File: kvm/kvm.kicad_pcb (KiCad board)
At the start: 4 copper layers, 56.8 x 69.3 mm, 61 parts, among them J1 USB4110-GF-A, J2 USB4110-GF-A, J3 USB_A_Stacked, J4 USB_A_Stacked, Q1 Q_PMOS_GSD, SW1 SW_DPDT_x2, U1 SRV05-4, U2 LTC4412xS6, U3 FSUSB42MUX, U4 GL850G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

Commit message: added gerber files
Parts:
- moved F2 2.03 mm to (92.2, 72.8), turned to -90 degrees
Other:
- board size 56.8 x 69.3 mm -> 57 x 69.3 mm
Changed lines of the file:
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@@
       (layerselection 0x00010fc_ffffffff)
       (disableapertmacros false)
-      (usegerberextensions false)
+      (usegerberextensions true)
       (usegerberattributes true)
-      (usegerberadvancedattributes true)
-      (creategerberjobfile true)
+      (usegerberadvancedattributes false)
+      (creategerberjobfile false)
       (svguseinch false)
       (svgprecision 6)
@@
       (plotinvisibletext false)
       (sketchpadsonfab false)
-      (subtractmaskfromsilk false)
+      (subtractmaskfromsilk true)
       (outputformat 1)
       (mirror false)
-      (drillshape 1)
+      (drillshape 0)
       (scaleselection 1)
-      (outputdirectory "")
+      (outputdirectory "fabrication/")
     )
   )
@@
     (fp_line (start -1.6 0.8) (end -1.6 -0.8) (layer "F.Fab") (width 0.1))
     (fp_line (start 1.6 0.8) (end -1.6 0.8) (layer "F.Fab") (width 0.1))
-    (pad "1" smd roundrect (at -1.4875 0 180) (size 1.425 1.75) (layers "F.Cu" "F.Paste" "F.Mask") (roundrect_rratio 0.175439)
+    (pad "1" smd roundrect (at -1.4875 0 180) (size 1.425 1.75) (layers "F.Cu" "F.Paste" "F.Mask") (roundrect_rratio 0.1754392982)
       (net 1 "V5") (pintype "passive"))
-    (pad "2" smd roundrect (at 1.4875 0 180) (size 1.425 1.75) (layers "F.Cu" "F.Paste" "F.Mask") (roundrect_rratio 0.175439)
+    (pad "2" smd roundrect (at 1.4875 0 180) (size 1.425 1.75) (layers "F.Cu" "F.Paste" "F.Mask") (roundrect_rratio 0.1754392982)
       (net 14 "Net-(C16-Pad1)") (pintype "passive"))
     (model "${KICAD6_3DMODEL_DIR}/Fuse.3dshapes/Fuse_1206_3216Metric.wrl"
@@
     (fp_line (start 1 0.625) (end -1 0.625) (layer "F.Fab") (width 0.1))
     (fp_line (start -1 -0.625) (end 1 -0.625) (layer "F.Fab") (width 0.1))
-    (pad "1" smd roundrect (at -1.0375 0 90) (size 1.175 1.45) (layers "F.Cu" "F.Paste" "F.Mask") (roundrect_rratio 0.212766)
+    (pad "1" smd roundrect (at -1.0375 0 90) (size 1.175 1.45) (layers "F.Cu" "F.Paste" "F.Mask") (roundrect_rratio 0.2127659574)
       (net 3 "DVDD") (pintype "passive"))
-    (pad "2" smd roundrect (at 1.0375 0 90) (size 1.175 1.45) (layers "F.Cu" "F.Paste" "F.Mask") (roundrect_rratio 0.212766)
+    (pad "2" smd roundrect (at 1.0375 0 90) (size 1.175 1.45) (layers "F.Cu" "F.Paste" "F.Mask") (roundrect_rratio 0.2127659574)
       (net 2 "GND") (pintype "passive"))
     (model "${KICAD6_3DMODEL_DIR}/Capacitor_SMD.3dshapes/C_0805_2012Metric.wrl"
@@
     (fp_line (start -1 0.6) (end 1 0.6) (layer "F.Fab") (width 0.1))
     (fp_line (start -1 -0.3) (end -1 0.6) (layer "F.Fab") (width 0.1))
-    (pad "1" smd roundrect (at -1.025 0) (size 1.15 1.4) (layers "F.Cu" "F.Paste" "F.Mask") (roundrect_rratio 0.217391)
+    (pad "1" smd roundrect (at -1.025 0) (size 1.15 1.4) (layers "F.Cu" "F.Paste" "F.Mask") (roundrect_rratio 0.2173913043)
       (net 17 "PGANG") (pinfunction "K") (pintype "passive"))
-    (pad "2" smd roundrect (at 1.025 0) (size 1.15 1.4) (layers "F.Cu" "F.Paste" "F.Mask") (roundrect_rratio 0.217391)
+    (pad "2" smd roundrect (at 1.025 0) (size 1.15 1.4) (layers "F.Cu" "F.Paste" "F.Mask") (roundrect_rratio 0.2173913043)
       (net 18 "Net-(D2-Pad2)") (pinfunction "A") (pintype "passive"))
     (model "${KICAD6_3DMODEL_DIR}/LED_SMD.3dshapes/LED_0805_2012Metric.wrl"
@@
     (fp_line (start -1.6 0.8) (end -1.6 -0.8) (layer "F.Fab") (width 0.1))
     (fp_line (start -1.6 -0.8) (end 1.6 -0.8) (layer "F.Fab") (width 0.1))
-    (pad "1" smd roundrect (at -1.4875 0 180) (size 1.425 1.75) (layers "F.Cu" "F.Paste" "F.Mask") (roundrect_rratio 0.175439)
+    (pad "1" smd roundrect (at -1.4875 0 180) (size 1.425 1.75) (layers "F.Cu" "F.Paste" "F.Mask") (roundrect_rratio 0.1754392982)
       (net 1 "V5") (pintype "passive"))
-    (pad "2" smd roundrect (at 1.4875 0 180) (size 1.425 1.75) (layers "F.Cu" "F.Paste" "F.Mask") (roundrect_rratio 0.175439)
+    (pad "2" smd roundrect (at 1.4875 0 180) (size 1.425 1.75) (layers "F.Cu" "F.Paste" "F.Mask") (roundrect_rratio 0.1754392982)
       (net 7 "Net-(C4-Pad1)") (pintype "passive"))
     (model "${KICAD6_3DMODEL_DIR}/Fuse.3dshapes/Fuse_1206_3216Metric.wrl"
@@
   )
   (footprint "Fuse:Fuse_1206_3216Metric_Pad1.42x1.75mm_HandSolder" (layer "F.Cu")
-    (at 93.599 74.23801 180)
+    (at 92.202 72.771 -90)
     (descr "Fuse SMD 1206 (3216 Metric), square (rectangular) end terminal, IPC_7351 nominal with elongated pad for handsoldering. (Body size source: http://www.tortai-tech.com/upload/download/2011102023233369053.pdf), generated with kicad-footprint-generator")
     (tags "fuse handsolder")
@@
     (property "Sheetname" "")
     (attr smd)
-    (fp_text reference "F2" (at 0 -1.82) (layer "F.SilkS")
+    (fp_text reference "F2" (at 0 -1.82 -270) (layer "F.SilkS")
       (effects (font (size 1 1) (thickness 0.15)))
     )
-    (fp_text value "Polyfuse" (at 0 1.82) (layer "F.Fab")
+    (fp_text value "Polyfuse" (at 0 1.82 -270) (layer "F.Fab")
       (effects (font (size 1 1) (thickness 0.15)))
     )
-    (fp_text user "${REFERENCE}" (at 0 0) (layer "F.Fab")
+    (fp_text user "${REFERENCE}" (at 0 0 -270) (layer "F.Fab")
       (effects (font (size 0.8 0.8) (thickness 0.12)))
     )
@@
     (fp_line (start -1.6 0.8) (end -1.6 -0.8) (layer "F.Fab") (width 0.1))
     (fp_line (start 1.6 0.8) (end -1.6 0.8) (layer "F.Fab") (width 0.1))
-    (pad "1" smd roundrect (at -1.4875 0 180) (size 1.425 1.75) (layers "F.Cu" "F.Paste" "F.Mask") (roundrect_rratio 0.175439)
+    (pad "1" smd roundrect (at -1.4875 0 270) (size 1.425 1.75) (layers "F.Cu" "F.Paste" "F.Mask") (roundrect_rratio 0.1754392982)
       (net 1 "V5") (pintype "passive"))
-    (pad "2" smd roundrect (at 1.4875 0 180) (size 1.425 1.75) (layers "F.Cu" "F.Paste" "F.Mask") (roundrect_rratio 0.175439)
+    (pad "2" smd roundrect (at 1.4875 0 270) (size 1.425 1.75) (layers "F.Cu" "F.Paste" "F.Mask") (roundrect_rratio 0.1754392982)
       (net 9 "Net-(C6-Pad1)") (pintype "passive"))
     (model "${KICAD6_3DMODEL_DIR}/Fuse.3dshapes/Fuse_1206_3216Metric.wrl"
@@
     (fp_line (start -1.6 0.8) (end -1.6 -0.8) (layer "F.Fab") (width 0.1))
     (fp_line (start -1.6 -0.8) (end 1.6 -0.8) (layer "F.Fab") (width 0.1))
-    (pad "1" smd roundrect (at -1.4875 0 180) (size 1.425 1.75) (layers "F.Cu" "F.Paste" "F.Mask") (roundrect_rratio 0.175439)
+    (pad "1" smd roundrect (at -1.4875 0 180) (size 1.425 1.75) (layers "F.Cu" "F.Paste" "F.Mask") (roundrect_rratio 0.1754392982)
       (net 1 "V5") (pintype "passive"))
-    (pad "2" smd roundrect (at 1.4875 0 180) (size 1.425 1.75) (layers "F.Cu" "F.Paste" "F.Mask") (roundrect_rratio 0.175439)
+    (pad "2" smd roundrect (at 1.4875 0 180) (size 1.425 1.75) (layers "F.Cu" "F.Paste" "F.Mask") (roundrect_rratio 0.1754392982)
       (net 15 "Net-(C17-Pad1)") (pintype "passive"))
     (model "${KICAD6_3DMODEL_DIR}/Fuse.3dshapes/Fuse_1206_3216Metric.wrl"
@@
     )
   )
-  (gr_rect (start 116.713 39.37) (end 59.944 108.712) (layer "Edge.Cuts") (width 0.1) (fill none))
+  (gr_rect (start 116.713 39.37) (end 59.69 108.712) (layer "Edge.Cuts") (width 0.1) (fill none))
   (gr_text "K(V)M - USB Hub\n" (at 104.394 42.926) (layer "F.SilkS")
     (effects (font (size 1.5 1.5) (thickness 0.3)))
@@
     (effects (font (size 1.5 1.5) (thickness 0.3)))
   )
+  (segment (start 92.202 71.2835) (end 92.202 69.469) (width 0.8) (layer "F.Cu") (net 1))
   (segment (start 81.915 48.514) (end 81.207512 48.514) (width 0.8) (layer "F.Cu") (net 1))
   (segment (start 85.524 48.3605) (end 85.3705 48.514) (width 0.8) (layer "F.Cu") (net 1))
-  (segment (start 95.0865 74.23801) (end 96.32299 74.23801) (width 0.8) (layer "F.Cu") (net 1))
   (segment (start 107.8821 59.0962) (end 109.4328 59.0962) (width 0.25) (layer "F.Cu") (net 1))
   (segment (start 109.4328 59.0962) (end 109.474 59.055) (width 0.25) (layer "F.Cu") (net 1))
@@
   (segment (start 88.4825 68.199) (end 90.043 68.199) (width 0.8) (layer "F.Cu") (net 1))
   (segment (start 81.1795 44.355908) (end 80.1665 43.342908) (width 0.8) (layer "F.Cu") (net 1))
-  (segment (start 96.32299 74.23801) (end 96.52 74.041) (width 0.8) (layer "F.Cu") (net 1))
   (segment (start 85.3705 48.514) (end 85.725 48.8685) (width 0.6) (layer "F.Cu") (net 1))
   (segment (start 81.1795 47.5985) (end 81.1795 44.355908) (width 0.8) (layer "F.Cu") (net 1))
@@
   (segment (start 86.1325 48.3605) (end 85.524 48.3605) (width 0.8) (layer "F.Cu") (net 1))
   (segment (start 92.1655 89.662) (end 93.853 89.662) (width 0.8) (layer "F.Cu") (net 1))
+  (via (at 92.202 69.469) (size 0.8) (drill 0.4) (layers "F.Cu" "B.Cu") (net 1))
   (via (at 86.868 83.947) (size 0.8) (drill 0.4) (layers "F.Cu" "B.Cu") (net 1))
   (via (at 112.776 89.916) (size 0.8) (drill 0.4) (layers "F.Cu" "B.Cu") (net 1))
@@
   (via (at 90.1965 42.2645) (size 0.8) (drill 0.4) (layers "F.Cu" "B.Cu") (net 1))
   (via (at 88.0375 48.2335) (size 0.8) (drill 0.4) (layers "F.Cu" "B.Cu") (net 1))
-  (via (at 96.52 74.041) (size 0.8) (drill 0.4) (layers "F.Cu" "B.Cu") (net 1))
   (via (at 96.266 95.25) (size 0.8) (drill 0.4) (layers "F.Cu" "B.Cu") (net 1))
   (via (at 108.712 75.311) (size 0.8) (drill 0.4) (layers "F.Cu" "B.Cu") (net 1))

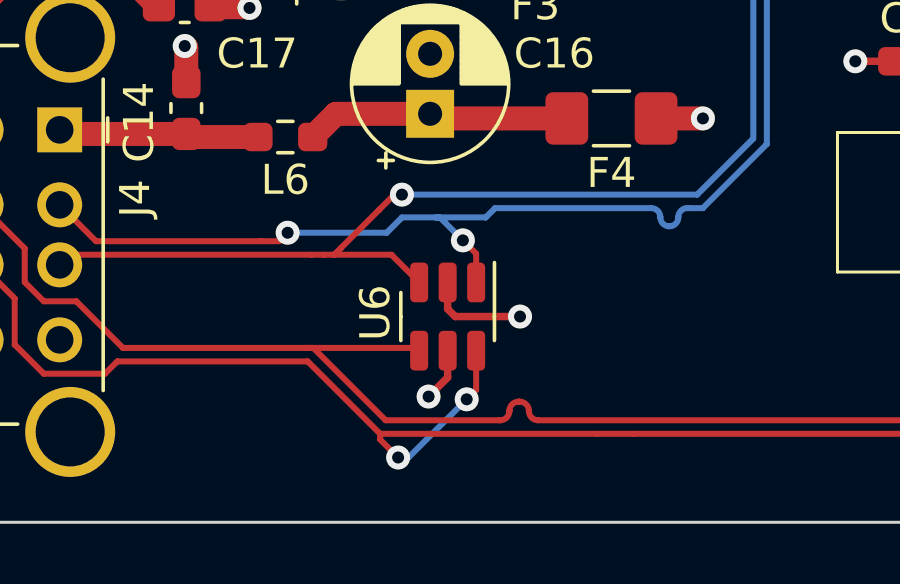
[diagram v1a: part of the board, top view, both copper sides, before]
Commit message: added mouser links to all components
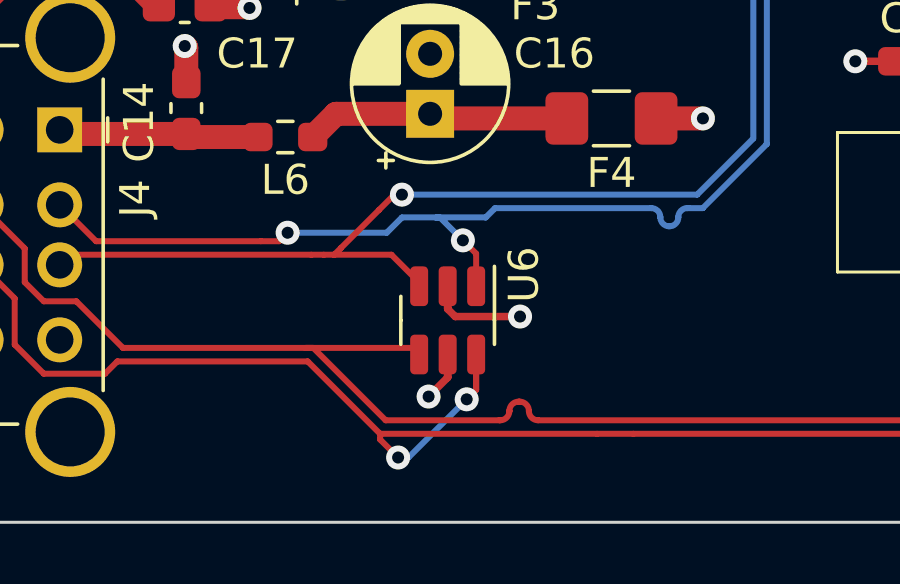
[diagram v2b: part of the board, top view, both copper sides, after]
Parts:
- moved U6 0.13 mm to (87.8, 102.0)
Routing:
- net D4+: track 71.3 -> 72.5 mm
- net V5: track 48.6 -> 49.4 mm
- net GND: track 72.4 -> 73.2 mm
